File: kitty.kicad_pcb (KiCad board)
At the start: 2 copper layers, 50.4 x 41.7 mm, 2 parts

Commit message: finish layout
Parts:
- removed the G*** at (0.00, 0.00) (x2)
- added ?: , kitty:p_logo_5_copper, F.Cu at (48.6, 54.2)
- added D1: LED, kitty:LED, B.Cu at (45.3, 36.6)
- added D2: LED, kitty:LED, B.Cu at (39.2, 41.4)
- added G*** (x2): LOGO, LOGO, F.Cu at (44.5, 40.6)
- added R1: 220R, Resistors_SMD:R_0805, B.Cu at (44.2, 45.9)
- added SAO1: 2x2, Pin_Headers:Pin_Header_Straight_2x02_Pitch2.54mm, B.Cu at (54.1, 53.3)
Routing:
- net Net-(D1-Pad1): track 0.00 -> 11.8 mm
- net GND: vias 0 -> 1
- added copper zone on B.Cu, net +3V3
- added copper zone on F.Cu, net GND

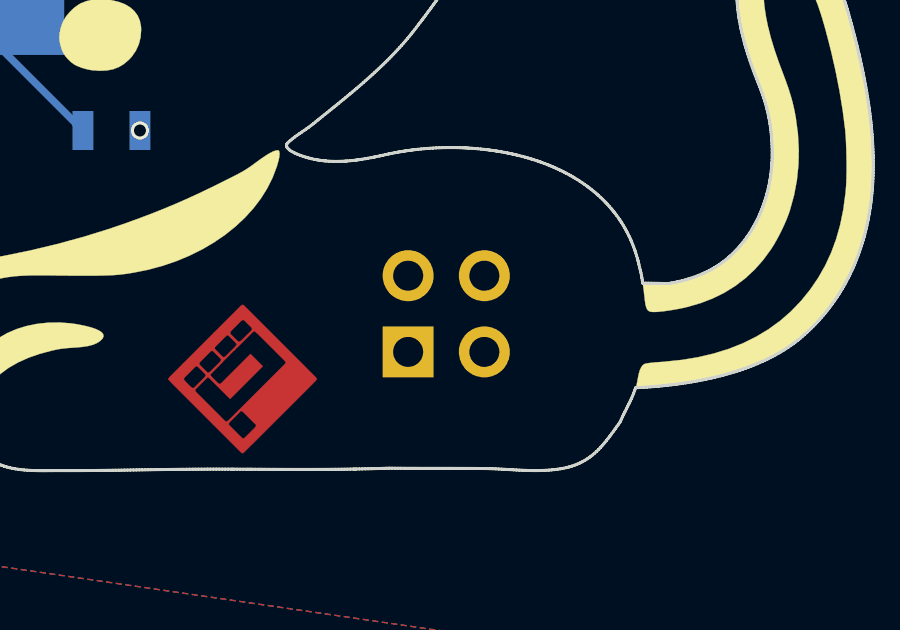
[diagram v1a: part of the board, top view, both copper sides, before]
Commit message: fix SAO header
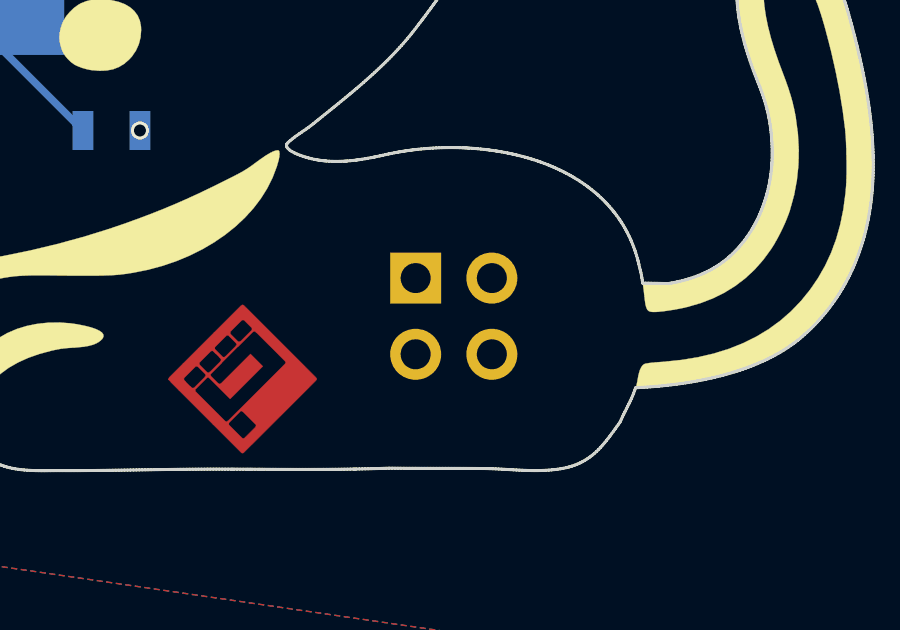
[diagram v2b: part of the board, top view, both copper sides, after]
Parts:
- removed the G*** at (44.5, 40.6) (x2)
- added G*** (x2): LOGO, LOGO, F.Cu at (44.5, 40.6)
- moved SAO1 2.47 mm to (54.3, 50.9), turned to 270 degrees
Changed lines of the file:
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@@
     (thickness 1.6)
     (drawings 2096)
-    (tracks 7)
+    (tracks 5)
     (zones 0)
     (modules 7)
@@
   )
   (module Pin_Headers:Pin_Header_Straight_2x02_Pitch2.54mm (layer B.Cu)
-    (at 54.09 53.31)
+    (at 54.34 50.85 270)
     (descr "Through hole straight pin header, 2x02, 2.54mm pitch, double rows")
     (tags "Through hole pin header THT 2x02 2.54mm double row")
-    (fp_text reference SAO1 (at 1.27 2.33) (layer B.SilkS)
+    (fp_text reference SAO1 (at 1.27 2.33 270) (layer B.SilkS)
       (effects (font (size 1 1) (thickness 0.15)) (justify mirror))
     )
-    (fp_text value 2x2 (at 1.27 -4.87) (layer B.Fab)
+    (fp_text value 2x2 (at 1.27 -4.87 270) (layer B.Fab)
       (effects (font (size 1 1) (thickness 0.15)) (justify mirror))
     )
@@
     (fp_line (start 4.35 -4.35) (end 4.35 1.8) (layer B.CrtYd) (width 0.05))
     (fp_line (start 4.35 1.8) (end -1.8 1.8) (layer B.CrtYd) (width 0.05))
-    (fp_text user %R (at 1.27 -1.27 270) (layer B.Fab)
+    (fp_text user %R (at 1.27 -1.27 540) (layer B.Fab)
       (effects (font (size 1 1) (thickness 0.15)) (justify mirror))
     )
-    (pad 1 thru_hole rect (at 0 0) (size 1.7 1.7) (drill 1) (layers *.Cu *.Mask)
+    (pad 1 thru_hole rect (at 0 0 270) (size 1.7 1.7) (drill 1) (layers *.Cu *.Mask)
       (net 1 +3V3))
-    (pad 2 thru_hole oval (at 2.54 0) (size 1.7 1.7) (drill 1) (layers *.Cu *.Mask)
+    (pad 2 thru_hole oval (at 2.54 0 270) (size 1.7 1.7) (drill 1) (layers *.Cu *.Mask)
       (net 3 GND))
-    (pad 3 thru_hole oval (at 0 -2.54) (size 1.7 1.7) (drill 1) (layers *.Cu *.Mask)
+    (pad 3 thru_hole oval (at 0 -2.54 270) (size 1.7 1.7) (drill 1) (layers *.Cu *.Mask)
       (net 4 "Net-(SAO1-Pad3)"))
-    (pad 4 thru_hole oval (at 2.54 -2.54) (size 1.7 1.7) (drill 1) (layers *.Cu *.Mask)
+    (pad 4 thru_hole oval (at 2.54 -2.54 270) (size 1.7 1.7) (drill 1) (layers *.Cu *.Mask)
       (net 5 "Net-(SAO1-Pad4)"))
     (model ${KISYS3DMOD}/Pin_Headers.3dshapes/Pin_Header_Straight_2x02_Pitch2.54mm.wrl
@@
   (gr_line (start 50.813151 15.569237) (end 50.813151 15.569237) (layer Edge.Cuts) (width 0.1))
   (gr_line (start 50.813151 15.569237) (end 50.812892 15.56907) (layer Edge.Cuts) (width 0.1))
-  (segment (start 54.09 53.31) (end 53.67 53.31) (width 0.25) (layer B.Cu) (net 1) (status C00000))
-  (segment (start 54.09 53.31) (end 54.1 53.31) (width 0.25) (layer B.Cu) (net 1) (status C00000))
   (segment (start 40.627 41.41) (end 40.627 43.307) (width 0.25) (layer B.Cu) (net 2))
   (segment (start 40.627 43.307) (end 43.25 45.93) (width 0.25) (layer B.Cu) (net 2))
